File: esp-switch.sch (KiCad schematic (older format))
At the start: 23 parts, among them J1 Conn_01x02, J2 Screw_Terminal_01x02, J3 Screw_Terminal_01x02, J4 Conn_01x04, U1 ATTINY441-SSU, U2 ESP-01v090, U3 MOC3041M, U4 MOC3041M

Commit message: Power supply added
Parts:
- removed J1: Conn_01x02, Pin_Headers:Pin_Header_Straight_1x02_Pitch2.54mm, symbol Conn_01x02
- added J5: Screw_Terminal_01x02, Connectors_Terminal_Blocks:TerminalBlock_Pheonix_MKDS1.5-2pol, symbol Screw_Terminal_01x02
- added U5: HLK-PM05, Power_Supply:HLK-PM05, symbol HLK-PM05
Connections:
- wire segments 71 -> 76
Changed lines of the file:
@@
 EESchema Schematic File Version 2
-LIBS:esp-switch-rescue
 LIBS:power
 LIBS:device
@@
 LIBS:valves
 LIBS:sensors
-LIBS:ESP8266
+LIBS:Power_Supplies
 LIBS:esp-switch-cache
 EELAYER 25 0
@@
 Wire Wire Line
 	6200 3000 6050 3000
-$Comp
-L Conn_01x02 J1
-U 1 1 59CBDAA0
-P 750 1100
-F 0 "J1" H 750 1200 50  0000 C CNN
-F 1 "Conn_01x02" H 750 900 50  0000 C CNN
-F 2 "Pin_Headers:Pin_Header_Straight_1x02_Pitch2.54mm" H 750 1100 50  0001 C CNN
-F 3 "" H 750 1100 50  0001 C CNN
-	1    750  1100
-	-1   0    0    -1
-$EndComp
-Wire Wire Line
-	950  1100 1500 1100
-Wire Wire Line
-	950  1200 1200 1200
-Wire Wire Line
-	1200 1200 1200 2500
 Wire Wire Line
 	1200 2300 1500 2300
 $Comp
-L +5V #PWR1
+L +5V #PWR01
 U 1 1 59CBDB7D
 P 1200 750
-F 0 "#PWR1" H 1200 600 50  0001 C CNN
+F 0 "#PWR01" H 1200 600 50  0001 C CNN
 F 1 "+5V" H 1200 890 50  0000 C CNN
 F 2 "" H 1200 750 50  0001 C CNN
@@
 $EndComp
 $Comp
-L GND #PWR2
+L GND #PWR02
 U 1 1 59CBDBC1
 P 1200 2500
-F 0 "#PWR2" H 1200 2250 50  0001 C CNN
+F 0 "#PWR02" H 1200 2250 50  0001 C CNN
 F 1 "GND" H 1200 2350 50  0000 C CNN
 F 2 "" H 1200 2500 50  0001 C CNN
@@
 	1    0    0    -1
 $EndComp
-Connection ~ 1200 2300
 Wire Wire Line
 	1200 1100 1200 750
-Connection ~ 1200 1100
-$Comp
-L GND #PWR4
+$Comp
+L GND #PWR03
 U 1 1 59CBDD84
 P 6500 2800
-F 0 "#PWR4" H 6500 2550 50  0001 C CNN
+F 0 "#PWR03" H 6500 2550 50  0001 C CNN
 F 1 "GND" H 6500 2650 50  0000 C CNN
 F 2 "" H 6500 2800 50  0001 C CNN
@@
 	6500 2700 6500 2800
 $Comp
-L +5V #PWR3
+L +5V #PWR04
 U 1 1 59CBDDB3
 P 4050 2400
-F 0 "#PWR3" H 4050 2250 50  0001 C CNN
+F 0 "#PWR04" H 4050 2250 50  0001 C CNN
 F 1 "+5V" H 4050 2540 50  0000 C CNN
 F 2 "" H 4050 2400 50  0001 C CNN
@@
 	4050 3000 4050 2400
 $Comp
-L GND #PWR5
+L GND #PWR05
 U 1 1 59CBE133
 P 7050 1500
-F 0 "#PWR5" H 7050 1250 50  0001 C CNN
+F 0 "#PWR05" H 7050 1250 50  0001 C CNN
 F 1 "GND" H 7050 1350 50  0000 C CNN
 F 2 "" H 7050 1500 50  0001 C CNN
@@
 $EndComp
 $Comp
-L +5V #PWR7
+L +5V #PWR06
 U 1 1 59CBE14F
 P 7500 900
-F 0 "#PWR7" H 7500 750 50  0001 C CNN
+F 0 "#PWR06" H 7500 750 50  0001 C CNN
 F 1 "+5V" H 7500 1040 50  0000 C CNN
 F 2 "" H 7500 900 50  0001 C CNN
@@
 $EndComp
 $Comp
-L GND #PWR8
+L GND #PWR07
 U 1 1 5A12EDB6
 P 8100 3850
-F 0 "#PWR8" H 8100 3600 50  0001 C CNN
+F 0 "#PWR07" H 8100 3600 50  0001 C CNN
 F 1 "GND" H 8100 3700 50  0000 C CNN
 F 2 "" H 8100 3850 50  0001 C CNN
@@
 $EndComp
 $Comp
-L GND #PWR9
+L GND #PWR08
 U 1 1 5A132AA4
 P 8100 5700
-F 0 "#PWR9" H 8100 5450 50  0001 C CNN
+F 0 "#PWR08" H 8100 5450 50  0001 C CNN
 F 1 "GND" H 8100 5550 50  0000 C CNN
 F 2 "" H 8100 5700 50  0001 C CNN
@@
 Connection ~ 7950 3750
 $Comp
-L +5V #PWR6
+L +5V #PWR09
 U 1 1 5A5584C2
 P 7400 3350
-F 0 "#PWR6" H 7400 3200 50  0001 C CNN
+F 0 "#PWR09" H 7400 3200 50  0001 C CNN
 F 1 "+5V" H 7400 3490 50  0000 C CNN
 F 2 "" H 7400 3350 50  0001 C CNN
@@
 Wire Wire Line
 	7400 3500 7400 3350
+$Comp
+L HLK-PM05 U5
+U 1 1 5A55884C
+P 9450 1550
+F 0 "U5" H 9300 1700 40  0000 C CNN
+F 1 "HLK-PM05" H 9450 1400 40  0000 C CNN
+F 2 "Power_Supply:HLK-PM05" H 8550 2900 60  0001 C CNN
+F 3 "" H 8550 2900 60  0000 C CNN
+	1    9450 1550
+	-1   0    0    -1
+$EndComp
+$Comp
+L Screw_Terminal_01x02 J5
+U 1 1 5A558F98
+P 10100 1500
+F 0 "J5" H 10100 1600 50  0000 C CNN
+F 1 "Screw_Terminal_01x02" H 10100 1700 50  0000 C CNN
+F 2 "Connectors_Terminal_Blocks:TerminalBlock_Pheonix_MKDS1.5-2pol" H 10100 1500 50  0001 C CNN
+F 3 "" H 10100 1500 50  0001 C CNN
+	1    10100 1500
+	1    0    0    -1
+$EndComp
+Wire Wire Line
+	9900 1500 9750 1500
+Wire Wire Line
+	9900 1600 9750 1600
+$Comp
+L GND #PWR010
+U 1 1 5A55918B
+P 9050 1700
+F 0 "#PWR010" H 9050 1450 50  0001 C CNN
+F 1 "GND" H 9050 1550 50  0000 C CNN
+F 2 "" H 9050 1700 50  0001 C CNN
+F 3 "" H 9050 1700 50  0001 C CNN
+	1    9050 1700
+	1    0    0    -1
+$EndComp
+$Comp
+L +5V #PWR011
+U 1 1 5A5591FA
+P 9050 1450
+F 0 "#PWR011" H 9050 1300 50  0001 C CNN
+F 1 "+5V" H 9050 1590 50  0000 C CNN
+F 2 "" H 9050 1450 50  0001 C CNN
+F 3 "" H 9050 1450 50  0001 C CNN
+	1    9050 1450
+	1    0    0    -1
+$EndComp
+Wire Wire Line
+	9150 1600 9050 1600
+Wire Wire Line
+	9050 1600 9050 1700
+Wire Wire Line
+	9150 1500 9050 1500
+Wire Wire Line
+	9050 1500 9050 1450
+Wire Wire Line
+	1200 2300 1200 2500
+Wire Wire Line
+	1200 1100 1500 1100
 $EndSCHEMATC

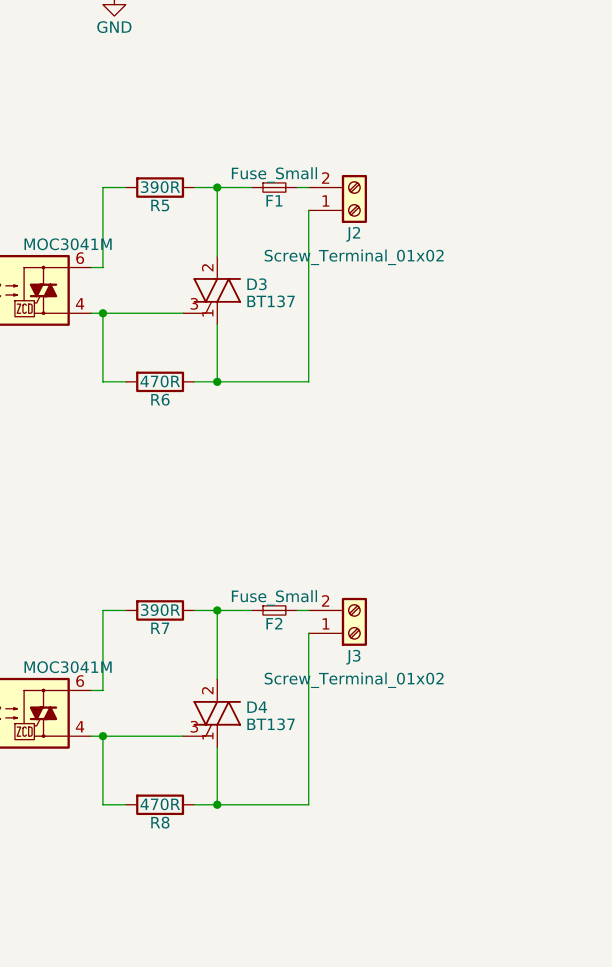
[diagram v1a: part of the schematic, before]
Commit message: Single switch source
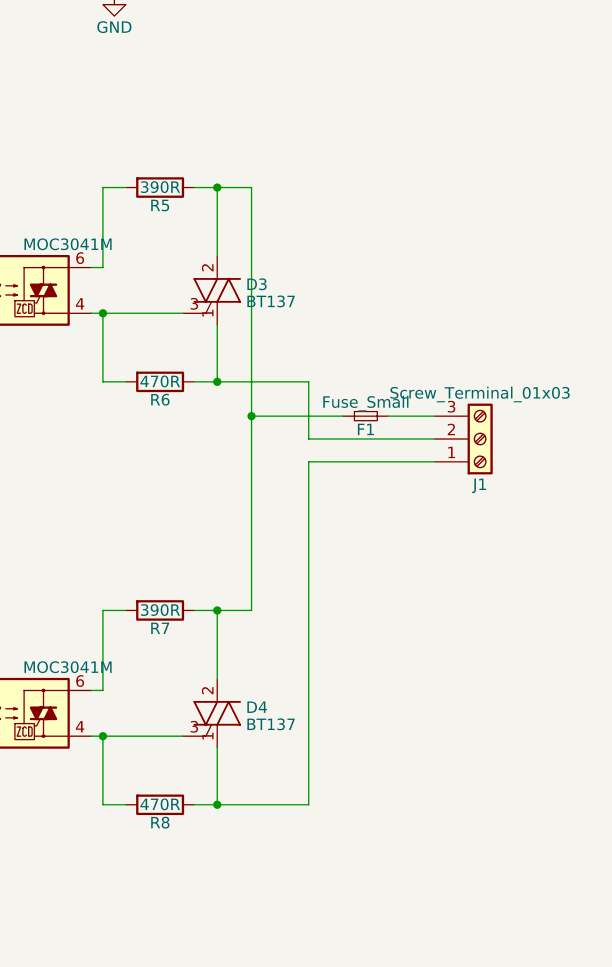
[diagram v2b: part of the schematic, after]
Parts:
- removed F2: Fuse_Small, Resistors_THT:R_Axial_DIN0411_L9.9mm_D3.6mm_P12.70mm_Horizontal, symbol Fuse_Small
- removed J2, J3: Screw_Terminal_01x02, Connectors_Terminal_Blocks:TerminalBlock_Pheonix_MKDS1.5-2pol, symbol Screw_Terminal_01x02
- added J1: Screw_Terminal_01x03, Connectors_Terminal_Blocks:TerminalBlock_Pheonix_MKDS1.5-3pol, symbol Screw_Terminal_01x03
- R6, R8: footprint Resistors_THT:R_Axial_DIN0411_L9.9mm_D3.6mm_P5.08mm_Vertical -> Resistors_THT:R_Axial_DIN0411_L9.9mm_D3.6mm_P7.62mm_Vertical
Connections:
- net at D3.1 (T1), R6.1: now also J1.2 (Pin_2)
- net at D3.2 (T2), F1.1, R5.1: now also D4.2 (T2), R7.1
- net at F1.2: now also J1.3 (Pin_3)
- net at D4.1 (T1), R8.1: now also J1.1 (Pin_1)
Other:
- moved on the sheet: F1
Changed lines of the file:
@@
 LIBS:valves
 LIBS:sensors
-LIBS:Power_Supplies
+LIBS:ESP8266
 LIBS:esp-switch-cache
 EELAYER 25 0
@@
 F 0 "R6" V 9330 3400 50  0000 C CNN
 F 1 "470R" V 9250 3400 50  0000 C CNN
-F 2 "Resistors_THT:R_Axial_DIN0411_L9.9mm_D3.6mm_P5.08mm_Vertical" V 9180 3400 50  0001 C CNN
+F 2 "Resistors_THT:R_Axial_DIN0411_L9.9mm_D3.6mm_P7.62mm_Vertical" V 9180 3400 50  0001 C CNN
 F 3 "" H 9250 3400 50  0001 C CNN
 	1    9250 3400
@@
 	9000 3400 9100 3400
 Connection ~ 9000 3100
-$Comp
-L Screw_Terminal_01x02 J2
-U 1 1 5A12FA42
-P 10100 2650
-F 0 "J2" H 10100 2750 50  0000 C CNN
-F 1 "Screw_Terminal_01x02" H 10100 2850 50  0000 C CNN
-F 2 "Connectors_Terminal_Blocks:TerminalBlock_Pheonix_MKDS1.5-2pol" H 10100 2650 50  0001 C CNN
-F 3 "" H 10100 2650 50  0001 C CNN
-	1    10100 2650
-	1    0    0    1
-$EndComp
 Wire Wire Line
 	8300 3100 8350 3100
@@
 	9500 2550 9500 2850
 Connection ~ 9500 2550
-Wire Wire Line
-	9900 2650 9900 3400
-Wire Wire Line
-	9900 3400 9400 3400
 $Comp
 L MOC3041M U4
@@
 F 0 "R8" V 9330 5250 50  0000 C CNN
 F 1 "470R" V 9250 5250 50  0000 C CNN
-F 2 "Resistors_THT:R_Axial_DIN0411_L9.9mm_D3.6mm_P5.08mm_Vertical" V 9180 5250 50  0001 C CNN
+F 2 "Resistors_THT:R_Axial_DIN0411_L9.9mm_D3.6mm_P7.62mm_Vertical" V 9180 5250 50  0001 C CNN
 F 3 "" H 9250 5250 50  0001 C CNN
 	1    9250 5250
@@
 	9000 5250 9100 5250
 Connection ~ 9000 4950
-$Comp
-L Screw_Terminal_01x02 J3
-U 1 1 5A132ACB
-P 10100 4500
-F 0 "J3" H 10100 4600 50  0000 C CNN
-F 1 "Screw_Terminal_01x02" H 10100 4700 50  0000 C CNN
-F 2 "Connectors_Terminal_Blocks:TerminalBlock_Pheonix_MKDS1.5-2pol" H 10100 4500 50  0001 C CNN
-F 3 "" H 10100 4500 50  0001 C CNN
-	1    10100 4500
-	1    0    0    1
-$EndComp
 Wire Wire Line
 	8300 4950 8350 4950
@@
 Connection ~ 9500 4400
 Wire Wire Line
-	9900 4500 9900 5250
-Wire Wire Line
 	9900 5250 9400 5250
-$Comp
-L Fuse_Small F1
-U 1 1 5A136B02
-P 9750 2550
-F 0 "F1" H 9750 2490 50  0000 C CNN
-F 1 "Fuse_Small" H 9750 2610 50  0000 C CNN
-F 2 "Resistors_THT:R_Axial_DIN0411_L9.9mm_D3.6mm_P12.70mm_Horizontal" H 9750 2550 50  0001 C CNN
-F 3 "" H 9750 2550 50  0001 C CNN
-	1    9750 2550
-	1    0    0    -1
-$EndComp
-Wire Wire Line
-	9900 2550 9850 2550
 Wire Wire Line
 	9650 2550 9400 2550
-$Comp
-L Fuse_Small F2
-U 1 1 5A136CC1
-P 9750 4400
-F 0 "F2" H 9750 4340 50  0000 C CNN
-F 1 "Fuse_Small" H 9750 4460 50  0000 C CNN
-F 2 "Resistors_THT:R_Axial_DIN0411_L9.9mm_D3.6mm_P12.70mm_Horizontal" H 9750 4400 50  0001 C CNN
-F 3 "" H 9750 4400 50  0001 C CNN
-	1    9750 4400
-	1    0    0    -1
-$EndComp
-Wire Wire Line
-	9900 4400 9850 4400
 Wire Wire Line
 	9650 4400 9400 4400
@@
 Wire Wire Line
 	1200 1100 1500 1100
+$Comp
+L Screw_Terminal_01x03 J1
+U 1 1 5A55A532
+P 10650 3650
+F 0 "J1" H 10650 3850 50  0000 C CNN
+F 1 "Screw_Terminal_01x03" H 10650 3450 50  0000 C CNN
+F 2 "Connectors_Terminal_Blocks:TerminalBlock_Pheonix_MKDS1.5-3pol" H 10650 3650 50  0001 C CNN
+F 3 "" H 10650 3650 50  0001 C CNN
+	1    10650 3650
+	1    0    0    1
+$EndComp
+Wire Wire Line
+	9900 3400 9400 3400
+$Comp
+L Fuse_Small F1
+U 1 1 5A136B02
+P 10150 3550
+F 0 "F1" H 10150 3490 50  0000 C CNN
+F 1 "Fuse_Small" H 10150 3610 50  0000 C CNN
+F 2 "Resistors_THT:R_Axial_DIN0411_L9.9mm_D3.6mm_P12.70mm_Horizontal" H 10150 3550 50  0001 C CNN
+F 3 "" H 10150 3550 50  0001 C CNN
+	1    10150 3550
+	1    0    0    -1
+$EndComp
+Wire Wire Line
+	9650 2550 9650 4400
+Wire Wire Line
+	10050 3550 9650 3550
+Connection ~ 9650 3550
+Wire Wire Line
+	10250 3550 10450 3550
+Wire Wire Line
+	9900 3400 9900 3650
+Wire Wire Line
+	9900 3650 10450 3650
+Wire Wire Line
+	9900 5250 9900 3750
+Wire Wire Line
+	9900 3750 10450 3750
 $EndSCHEMATC

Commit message: Complete layout
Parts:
- removed RF1: RF_Receiver_433_MHz, Sensors:RF_Receiver_433_MHz, symbol RF_Receiver_433_MHz
- added J2: Conn_01x04, Pin_Headers:Pin_Header_Straight_1x04_Pitch2.54mm, symbol Conn_01x04
- added RF1: RF_Receiver_EV1527, footprints:RF_Receiver_Decoder, symbol RF_Receiver_EV1527
- D3, D4: symbol Q_TRIAC_AAG-RESCUE-esp-switch -> TRIAC_TTG
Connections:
- net +5V: now also U2.3 (CH_PD), U2.5 (RST), RF1.2 (VDD)
- net GND: now also RF1.1 (GND)
- net at U1.10 ((PCINT3/SCK/XCK0/T0/TOCC2/AIN10/ADC3)PA3): now also RF1.4 (D1), RF1.5 (D2)
- net at U1.13 ((PCINT0/MISO/AREF/ADC0)PA0): now also RF1.3 (D0), RF1.6 (D3)
- net at U1.2 ((PCINT8/CLKI/XTAL1/ADC11)PB0): now also D1.2 (A), J4.1 (Pin_1), U3.1
- net at U1.3 ((PCINT9/INT0/XTAL2/ADC10)PB1): now also D2.2 (A), J4.2 (Pin_2), U4.1
- net at U1.4 ((PCINT11/dW/~RESET~/ADC9)PB3): now also J2.4 (Pin_4)
- net at U1.5 ((PCINT10/RXD0/ICP2/CLKO/TOCC7/ADC8)PB2): now also RF1.8 (SW)
- net at U1.6 ((PCINT7/~SS~/TXD0/ICP1/TOCC6/ADC7)PA7): now also RF1.7 (VT)
- net at U1.7 ((PCINT6/MOSI/SDA/XCK1/TOCC5/ACO1/ADC6)PA6): now also J2.3 (Pin_3)
- net at U1.8 ((PCINT5/MISO/TXD1/T2/TOCC4/ACO0/ADC5)PA5): now also J2.2 (Pin_2)
- net at U1.9 ((PCINT4/SCK/SCL/RXD1/T1/TOCC3/AIN11/ADC4)PA4): now also J2.1 (Pin_1)
- no-connect marks 2 -> 3
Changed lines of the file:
@@
 LIBS:sensors
 LIBS:ESP8266
+LIBS:triac_ttg
+LIBS:hlk-pm05
 LIBS:esp-switch-cache
 EELAYER 25 0
@@
 $EndComp
 $Comp
-L RF_Receiver_433_MHz RF1
-U 1 1 59CBD604
-P 6850 1200
-F 0 "RF1" H 6850 1850 60  0000 C CNN
-F 1 "RF_Receiver_433_MHz" H 6850 1750 60  0000 C CNN
-F 2 "Sensors:RF_Receiver_433_MHz" H 6950 1200 60  0001 C CNN
-F 3 "" H 6950 1200 60  0000 C CNN
-	1    6850 1200
-	1    0    0    -1
-$EndComp
-$Comp
 L ESP-01v090 U2
 U 1 1 59CBD699
@@
 	3950 1300 3600 1300
 Wire Wire Line
-	3600 1200 6200 1200
-Wire Wire Line
-	6200 1200 6200 3000
-Wire Wire Line
 	6200 3000 6050 3000
 Wire Wire Line
@@
 L +5V #PWR04
 U 1 1 59CBDDB3
-P 4050 2400
-F 0 "#PWR04" H 4050 2250 50  0001 C CNN
-F 1 "+5V" H 4050 2540 50  0000 C CNN
-F 2 "" H 4050 2400 50  0001 C CNN
-F 3 "" H 4050 2400 50  0001 C CNN
-	1    4050 2400
+P 4050 2500
+F 0 "#PWR04" H 4050 2350 50  0001 C CNN
+F 1 "+5V" H 4050 2640 50  0000 C CNN
+F 2 "" H 4050 2500 50  0001 C CNN
+F 3 "" H 4050 2500 50  0001 C CNN
+	1    4050 2500
 	1    0    0    -1
 $EndComp
 Wire Wire Line
 	4150 3000 4050 3000
-Wire Wire Line
-	4050 3000 4050 2400
 $Comp
 L GND #PWR05
 U 1 1 59CBE133
-P 7050 1500
-F 0 "#PWR05" H 7050 1250 50  0001 C CNN
-F 1 "GND" H 7050 1350 50  0000 C CNN
-F 2 "" H 7050 1500 50  0001 C CNN
-F 3 "" H 7050 1500 50  0001 C CNN
-	1    7050 1500
+P 7350 1600
+F 0 "#PWR05" H 7350 1350 50  0001 C CNN
+F 1 "GND" H 7350 1450 50  0000 C CNN
+F 2 "" H 7350 1600 50  0001 C CNN
+F 3 "" H 7350 1600 50  0001 C CNN
+	1    7350 1600
 	1    0    0    -1
 $EndComp
@@
 L +5V #PWR06
 U 1 1 59CBE14F
-P 7500 900
-F 0 "#PWR06" H 7500 750 50  0001 C CNN
-F 1 "+5V" H 7500 1040 50  0000 C CNN
-F 2 "" H 7500 900 50  0001 C CNN
-F 3 "" H 7500 900 50  0001 C CNN
-	1    7500 900
-	1    0    0    -1
-$EndComp
-Wire Wire Line
-	6750 1200 6750 1300
-Wire Wire Line
-	6750 1300 7500 1300
-Wire Wire Line
-	7500 1300 7500 900
-Wire Wire Line
-	7050 1200 7050 1500
+P 7100 900
+F 0 "#PWR06" H 7100 750 50  0001 C CNN
+F 1 "+5V" H 7100 1040 50  0000 C CNN
+F 2 "" H 7100 900 50  0001 C CNN
+F 3 "" H 7100 900 50  0001 C CNN
+	1    7100 900
+	1    0    0    -1
+$EndComp
 $Comp
 L MOC3041M U3
@@
 	7150 2550 8350 2550
 $Comp
-L Q_TRIAC_AAG-RESCUE-esp-switch D3
+L TRIAC_TTG D3
 U 1 1 5A12F072
 P 9500 3000
@@
 	8350 4400 8350 4750
 Wire Wire Line
-	7150 4400 8350 4400
-$Comp
-L Q_TRIAC_AAG-RESCUE-esp-switch D4
+	6700 4400 8350 4400
+$Comp
+L TRIAC_TTG D4
 U 1 1 5A132AB3
 P 9500 4850
@@
 $EndComp
 Wire Wire Line
-	7050 3300 7150 3300
-Wire Wire Line
-	7150 3300 7150 2550
+	7150 3300 7050 3300
+Wire Wire Line
+	7150 2000 7150 3300
 Wire Wire Line
 	7050 3400 7150 3400
@@
 Wire Wire Line
 	9900 3750 10450 3750
+$Comp
+L RF_Receiver_EV1527 RF1
+U 1 1 5A625B90
+P 7750 1100
+F 0 "RF1" H 7900 1400 60  0000 C CNN
+F 1 "RF_Receiver_EV1527" H 7750 1550 60  0000 C CNN
+F 2 "footprints:RF_Receiver_Decoder" H 7650 1100 60  0001 C CNN
+F 3 "" H 7650 1100 60  0001 C CNN
+	1    7750 1100
+	1    0    0    -1
+$EndComp
+Wire Wire Line
+	6200 3000 6200 3300
+Wire Wire Line
+	6200 3300 3850 3300
+Wire Wire Line
+	3850 3300 3850 1200
+Wire Wire Line
+	3850 1200 3600 1200
+Wire Wire Line
+	7450 1350 7450 1400
+Wire Wire Line
+	7450 1400 7100 1400
+Wire Wire Line
+	7100 1400 7100 900
+Wire Wire Line
+	7550 1350 7550 1450
+Wire Wire Line
+	5100 1450 7850 1450
+Wire Wire Line
+	7850 1450 7850 1350
+Wire Wire Line
+	7750 1550 7750 1350
+Wire Wire Line
+	5000 1550 7750 1550
+Wire Wire Line
+	7650 1550 7650 1350
+$Comp
+L Conn_01x04 J2
+U 1 1 5A635AA5
+P 4750 750
+F 0 "J2" H 4750 950 50  0000 C CNN
+F 1 "Conn_01x04" H 4750 450 50  0000 C CNN
+F 2 "Pin_Headers:Pin_Header_Straight_1x04_Pitch2.54mm" H 4750 750 50  0001 C CNN
+F 3 "" H 4750 750 50  0001 C CNN
+	1    4750 750
+	1    0    0    -1
+$EndComp
+Wire Wire Line
+	3600 1500 4100 1500
+Wire Wire Line
+	4100 1500 4100 650
+Wire Wire Line
+	4100 650  4550 650
+Wire Wire Line
+	3600 1600 4150 1600
+Wire Wire Line
+	4150 1600 4150 750
+Wire Wire Line
+	4150 750  4550 750
+Wire Wire Line
+	3600 1700 4200 1700
+Wire Wire Line
+	4200 1700 4200 850
+Wire Wire Line
+	4200 850  4550 850
+Wire Wire Line
+	3600 2300 4250 2300
+Wire Wire Line
+	4250 2300 4250 950
+Wire Wire Line
+	4250 950  4550 950
+Wire Wire Line
+	4050 3000 4050 2500
+Wire Wire Line
+	3600 1100 5100 1100
+Wire Wire Line
+	5100 1100 5100 1450
+Connection ~ 7550 1450
+Wire Wire Line
+	3600 1400 5000 1400
+Wire Wire Line
+	5000 1400 5000 1550
+Connection ~ 7650 1550
+Wire Wire Line
+	3600 1800 7950 1800
+Wire Wire Line
+	7950 1800 7950 1350
+Wire Wire Line
+	7350 1600 7350 1350
+Wire Wire Line
+	3600 2000 7150 2000
+Connection ~ 7150 2550
+Wire Wire Line
+	3600 2100 6700 2100
+Wire Wire Line
+	6700 2100 6700 4400
+Connection ~ 7150 4400
+Wire Wire Line
+	3600 2200 8050 2200
+Wire Wire Line
+	8050 2200 8050 1350
+NoConn ~ 8150 1350
+Wire Wire Line
+	4150 2800 4050 2800
+Connection ~ 4050 2800
+Wire Wire Line
+	4150 2900 4050 2900
+Connection ~ 4050 2900
 $EndSCHEMATC
